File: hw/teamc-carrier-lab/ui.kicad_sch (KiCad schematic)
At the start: 20 parts, among them J10 GO/STOP button, J11 role toggle, J12 mode toggle, U11 SP0504BAHTG

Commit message: Carrier rev B (UPC lab): placed and routed on one copper layer, DRC 0/0/0
- place_carrier_lab.py: fixed floorplan (power right, J1 centre, SP4 socket top-left
  edge, UI leads left edge, fuel gauge bottom-left); provisional 100 x 80 mm outline
  until the box is measured.
- linkroute.py: single-layer grid router whose second "layer" is straight wire links
  (bare wire on the component side between two unplated holes).
- route_carrier_lab.py: hand-coded power path, SCK swap under R84/R83, left half; the
  rest routed in a topology order, --search over the band-net orders.
- finish_carrier_lab.py: GND pour (0.4 mm), FR10 no-fill areas, M3 keep-outs, ground
  island joins, links -> W parts (one-pin symbol, WireLink footprint with jumper pads).
- fab_carrier_lab.py: F.Cu + Edge.Cuts gerbers, drill, 1:1 copper PDFs, assembly and
  schematic PDFs, zip; renders; build_bom.py --rev b -> hw/BOM_revB.csv (~EUR 139).
- Schematic changes for one layer (documented on the sheets and in DESIGN_NOTES):
  1206 R/C, no UI pull-ups, 4 x SMF5.0A instead of SP0504, R80 to 3V3_RADIO, no R81,
  no C71/TP10/TP2 (C12 10 uF), 3V3_PI from J1 pin 1, FG_ALRT not routed, LED return
  on pin 25, J1 GND pins 20/30/34/39 unused, J23 on BAT_IN.
- ERC 0; DRC 0 violations / 0 unconnected / 0 parity (silk/mask checks off: the lab
  board has neither); 10 wire links (138 mm).

Co-Authored-By: Claude Opus 5.5 <noreply@anthropic.com>
Claude-Session: https://claude.ai/code/session_01M3xdFsssmBw3o2iBWKaKwo
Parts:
- removed R50, R51, R52, R53: 10k, Resistor_SMD:R_0805_2012Metric_Pad1.20x1.40mm_HandSolder, symbol Device:R
- removed U11: SP0504BAHTG, Package_TO_SOT_SMD:SOT-23-5, symbol Power_Protection:SP0504BAHT
- added D12, D13, D14, D15: SMF5.0A, Diode_SMD:D_SMF, symbol Diode:SMF5V0A
- C50, C51, C52, C53: footprint Capacitor_SMD:C_0805_2012Metric_Pad1.18x1.45mm_HandSolder -> Capacitor_SMD:C_1206_3216Metric_Pad1.33x1.80mm_HandSolder; MPN CL21B104KBCNNNC -> CL31B104KBCNNNC
- R54, R55, R56, R57: footprint Resistor_SMD:R_0805_2012Metric_Pad1.20x1.40mm_HandSolder -> Resistor_SMD:R_1206_3216Metric_Pad1.30x1.75mm_HandSolder; MPN RC0805FR-071KL -> RC1206FR-071KL
- R60, R61: footprint Resistor_SMD:R_0805_2012Metric_Pad1.20x1.40mm_HandSolder -> Resistor_SMD:R_1206_3216Metric_Pad1.30x1.75mm_HandSolder; MPN RC0805FR-07330RL -> RC1206FR-07330RL
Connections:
- net BTN_TXRX_J: now also D12.1 (A1)
- net GND: now also D12.2 (A2), D13.2 (A2), D14.2 (A2), D15.2 (A2); no longer D10.1 (K), D11.1 (K)
- net SW_MODE_MRM_J: now also D15.1 (A1)
- net SW_MODE_NM_J: now also D14.1 (A1)
- net SW_ROLE_J: now also D13.1 (A1)
- new net LED_RTN: D10.1 (K), D11.1 (K)
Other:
- note added: "D10 activity (GPIO 5), D11 status (GPIO 6). (3.3 − ~2.0 V) / 330 Ω ≈ 4 mA, well under the Pi's 16 mA per pin. No InGaN (blue/white: Vf too high). Rev B: the cathodes return on LED_RTN = J1 pin 25 (a Pi GND pin) - on one copper layer the LEDs sit in a pocket of J1's escape tracks, away from the carrier's pour."
- note added: "DRAFT – for ET review. Software: proto/port/linux/ui.c (inputs active low with the Pi's pull-ups; LEDs active high). Mode switch (J12, ON-OFF-ON): GPIO 23 low = NM, else GPIO 16 low = MRM, else (centre) SRI. Role (J11): low = TX. Pull-ups: the Pi's own (ui.c); rev A's external 10 kΩ are gone in rev B (one copper layer). 1 kΩ series: GPIO 16 may be driven by legacy firmware at boot (HAT design gui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"
- note added: "ESD (one TVS per lead, at the connectors)"
- note added: "NO EXTERNAL PULL-UPS IN REV B (R50-R53 of rev A)"
- note added: "Rev B: four SMF5.0A (5 V standoff, 200 W, pin 1 = cathode to the line), the part already used for D2/D3, instead of rev A's SP0504 4-line array: on one copper layer a single SOT-23-5 cannot reach four parallel lead lines without a crossing. The TVS capacitance (~1 nF) sits before the 1 kΩ / 100 nF filter: harmless."
- note added: "The inputs use the Pi's pull-ups, which ui.c requests (GPIO_V2_LINE_FLAG_BIAS_PULL_UP) before it reads them. Until then (boot) the BCM2837 default pull-down makes an open toggle read 'active' - nothing reads them then. On one copper layer a 3V3 bus to four pull-ups at the leads cuts the ground pour into islands."
- note removed: "4-line TVS array, 5.5 V standoff, 30 pF, ≤ 100 nA leakage (datasheet p.2), IEC 61000-4-2 20 kV contact. Pin 2 = common → GND; 1/3/4/5 = lines (datasheet p.1)."
- note removed: "D10 activity (GPIO 5), D11 status (GPIO 6). (3.3 − ~2.0 V) / 330 Ω ≈ 4 mA, well under the Pi's 16 mA per pin. No InGaN (blue/white: Vf too high)."
- note removed: "DRAFT – for ET review. Software: proto/port/linux/ui.c (inputs active low with the Pi's pull-ups; LEDs active high). Mode switch (J12, ON-OFF-ON): GPIO 23 low = NM, else GPIO 16 low = MRM, else (centre) SRI. Role (J11): low = TX. External 10 kΩ pull-ups: the BCM2837 boot default on GPIO 16/17/23/27 is a PULL-DOWN, so an open toggle would read 'active' until Linux sets the pull-up. 1 kΩ series: GP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"
- note removed: "ESD (at the connectors)"
- note removed: "PULL-UP 10 kΩ (connector side)"

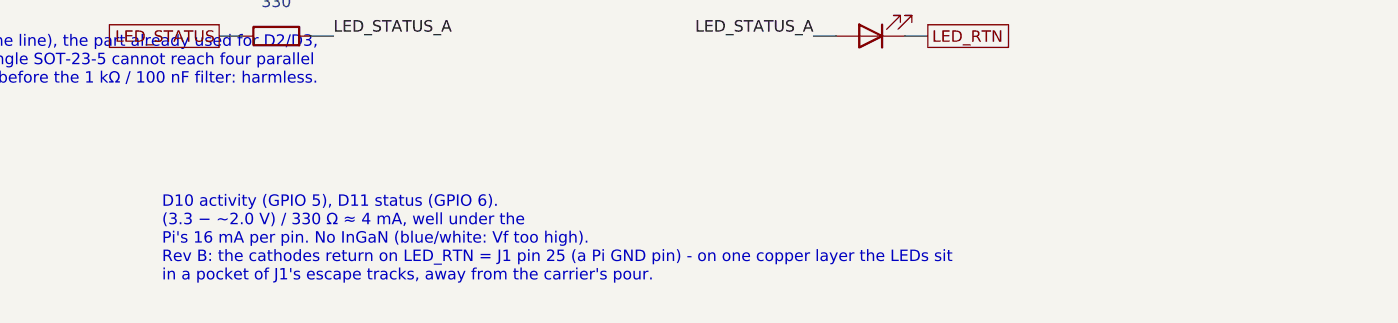
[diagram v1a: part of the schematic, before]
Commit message: Carrier rev B review fixes: charger on VBAT, insulated links, SPI at 4 MHz
- J23 (TP4056 lead) back on VBAT behind F1/Q1: placed between the VBAT line and
  C5, GND to C5's ground pad, R1 now returns to J20's GND pin. A reversed cell no
  longer reaches the charger and the lead is fused.
- Wire links: insulated 22 AWG solid hook-up wire, not bare (schematic note, W
  MPN, WireLink footprint text, BoM, shopping list).
- Ribbon grounds: tying J1 20/25 to the pour was tried; the inner pocket of J1's
  escape ring (LEDs, pins 20/25) has no legal wire link, the outer pockets would
  cost 3 more. Kept as before and SPI defaults to 4 MHz instead (teamc-node
  --spi-hz, NRF24_LINUX_CFG_DEFAULT; was 8 MHz) until T2 is clean; flying-wire
  fallback documented.
- Pipeline rerun twice: ERC 0, DRC 0/0/0, one copper layer, no vias, 10 links;
  fab zip, 1:1 PDFs, renders and BOM_revB.csv (EUR 139.01) regenerated.
- fw 318, proto all scenarios + 116 usb, linux builds, phy_config OK.

Co-Authored-By: Claude Opus 5.5 <noreply@anthropic.com>
Claude-Session: https://claude.ai/code/session_01PKzvcoWGaf5niy6TrXYsya
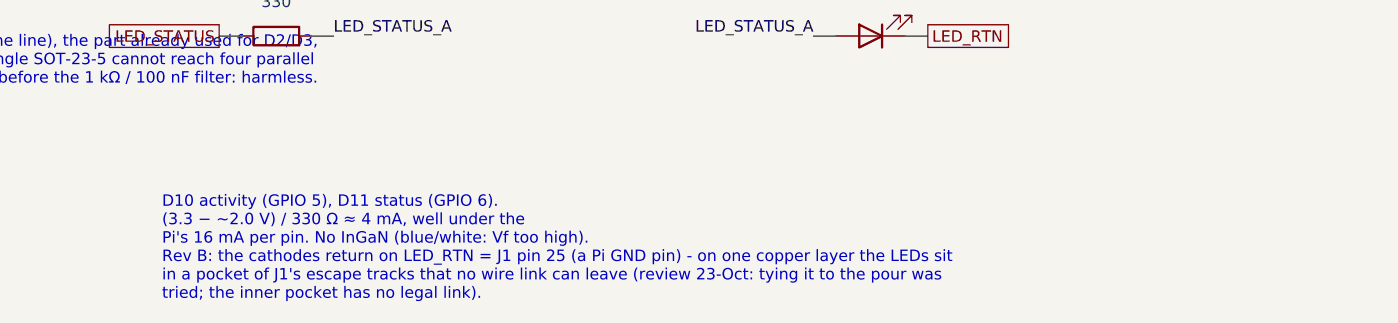
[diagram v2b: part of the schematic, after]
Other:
- note added: "D10 activity (GPIO 5), D11 status (GPIO 6). (3.3 − ~2.0 V) / 330 Ω ≈ 4 mA, well under the Pi's 16 mA per pin. No InGaN (blue/white: Vf too high). Rev B: the cathodes return on LED_RTN = J1 pin 25 (a Pi GND pin) - on one copper layer the LEDs sit in a pocket of J1's escape tracks that no wire link can leave (review 23-Oct: tying it to the pour was tried; the inner pocket has no legal link)."
- note removed: "D10 activity (GPIO 5), D11 status (GPIO 6). (3.3 − ~2.0 V) / 330 Ω ≈ 4 mA, well under the Pi's 16 mA per pin. No InGaN (blue/white: Vf too high). Rev B: the cathodes return on LED_RTN = J1 pin 25 (a Pi GND pin) - on one copper layer the LEDs sit in a pocket of J1's escape tracks, away from the carrier's pour."
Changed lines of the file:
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@@
 		)
 	)
-	(text "D10 activity (GPIO 5), D11 status (GPIO 6).\n(3.3 − ~2.0 V) / 330 Ω ≈ 4 mA, well under the\nPi's 16 mA per pin. No InGaN (blue/white: Vf too high).\nRev B: the cathodes return on LED_RTN = J1 pin 25 (a Pi GND pin) - on one copper layer the LEDs sit\nin a pocket of J1's escape tracks, away from the carrier's pour."
+	(text "D10 activity (GPIO 5), D11 status (GPIO 6).\n(3.3 − ~2.0 V) / 330 Ω ≈ 4 mA, well under the\nPi's 16 mA per pin. No InGaN (blue/white: Vf too high).\nRev B: the cathodes return on LED_RTN = J1 pin 25 (a Pi GND pin) - on one copper layer the LEDs sit\nin a pocket of J1's escape tracks that no wire link can leave (review 23-Oct: tying it to the pour was\ntried; the inner pocket has no legal link)."
 		(exclude_from_sim no)
 		(at 208.28 233.68 0)
